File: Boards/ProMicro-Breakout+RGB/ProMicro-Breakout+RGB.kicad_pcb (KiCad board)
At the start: 2 copper layers, 76.2 x 43.2 mm, 23 parts, among them J1 Conn_01x04, J10 Conn_01x12, J11 Conn_01x02, J12 Conn_01x02, J13 Conn_01x02, J14 Conn_01x02, J15 Conn_01x02, J16 Conn_01x02, J17 Conn_01x02, J18 Conn_01x04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

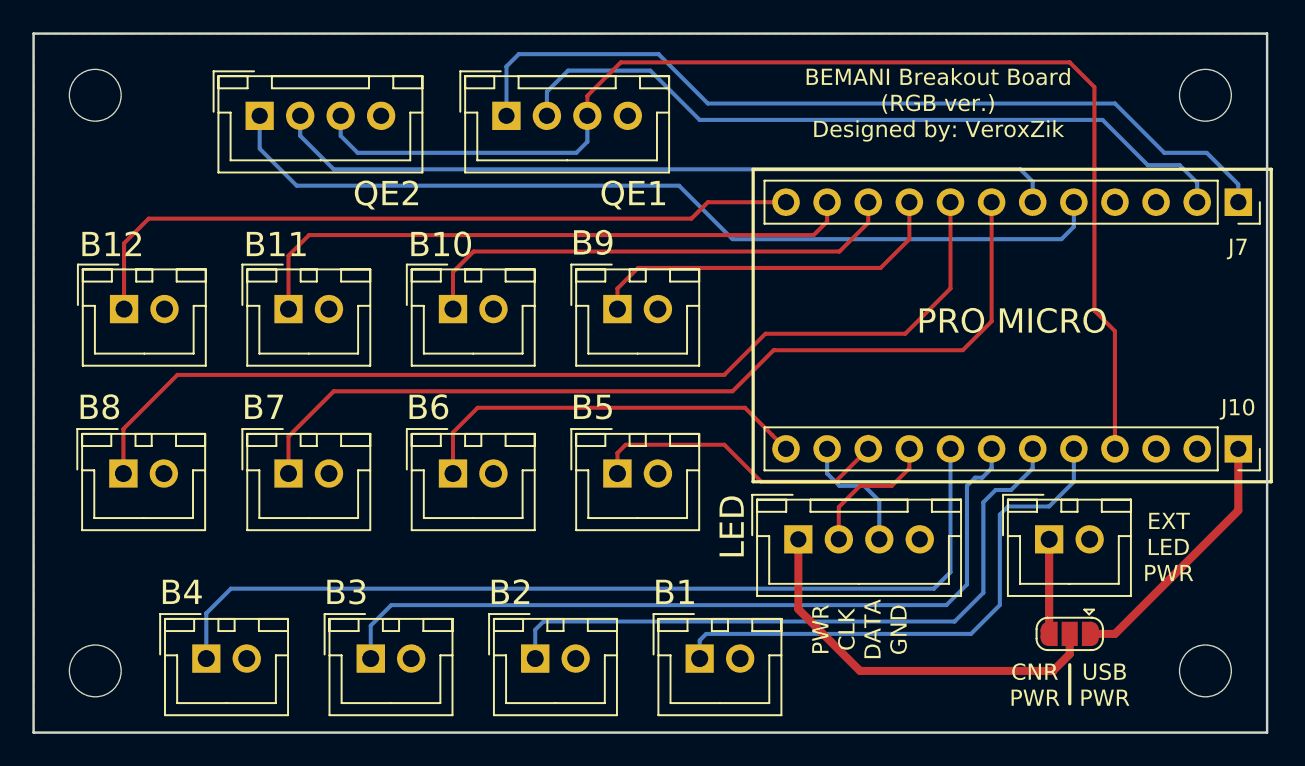
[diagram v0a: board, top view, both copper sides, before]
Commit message: Update ProMicro-Breakout+RGB board.
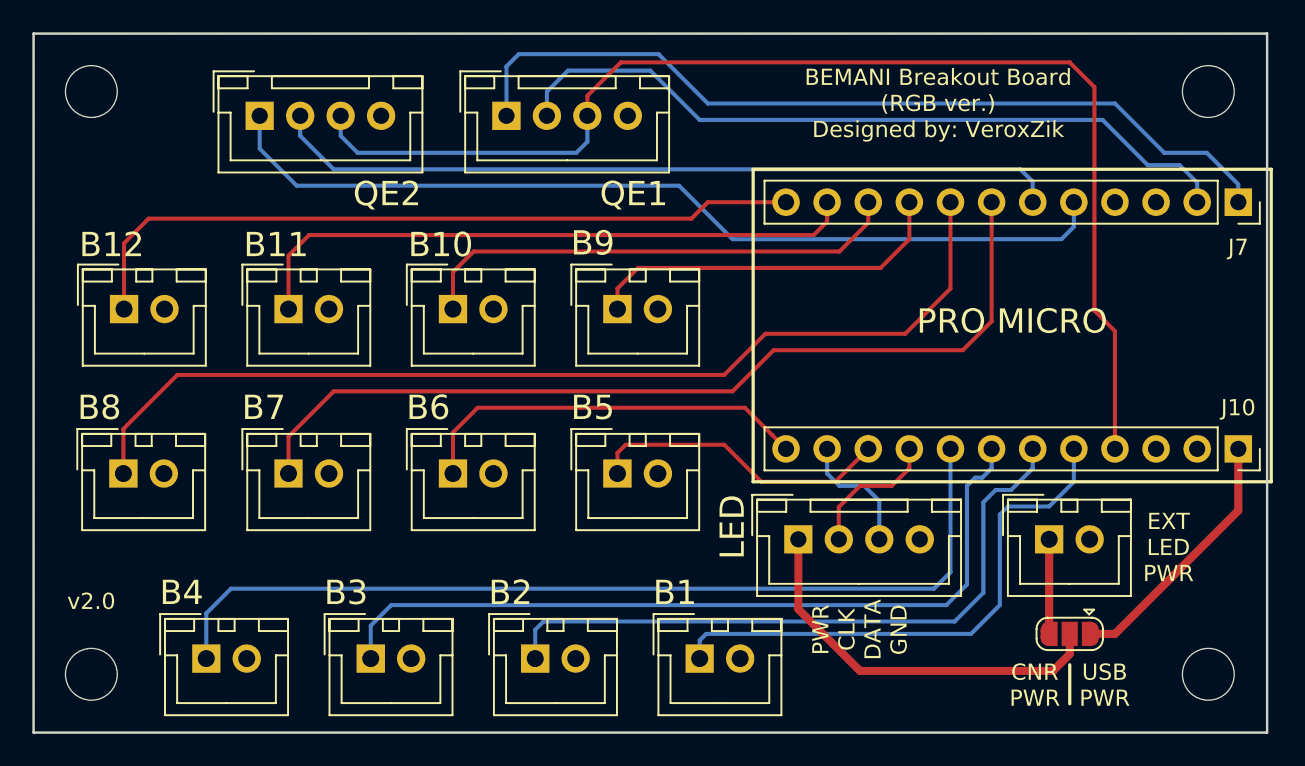
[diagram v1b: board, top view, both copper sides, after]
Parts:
- moved MH2 0.33 mm to (110.2, 93.8)
- moved MH1 0.32 mm to (110.2, 129.8)
- moved MH4 0.29 mm to (179.2, 93.8)
- moved MH3 0.28 mm to (179.2, 129.8)
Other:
- net class Default removed
- rule pad_to_mask_clearance: 0.2 -> 0
- board text added: "v2.0"
